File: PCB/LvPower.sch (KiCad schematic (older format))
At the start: 19 parts

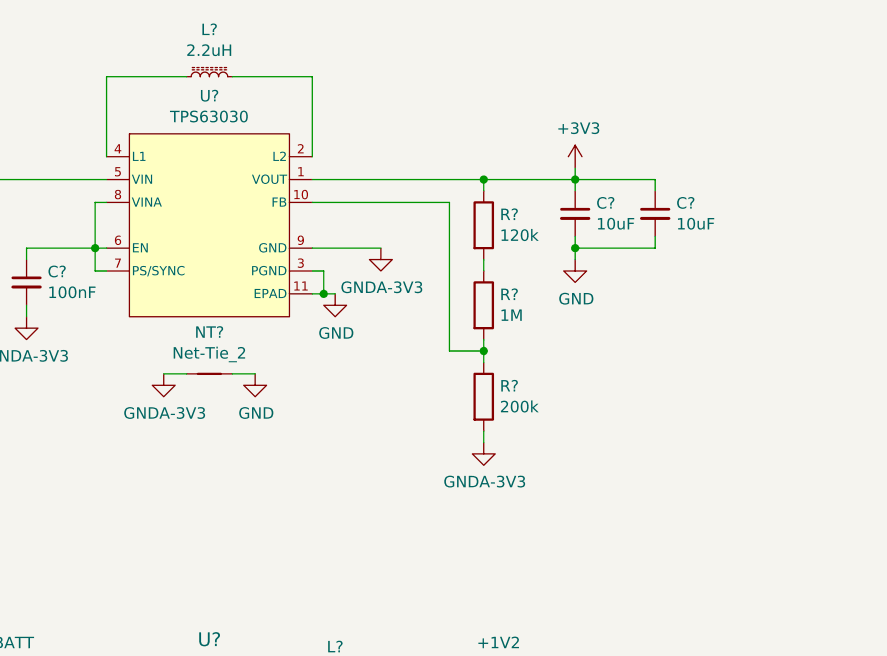
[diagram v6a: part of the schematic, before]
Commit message: Change TPS63030 to TPS63031 to reduce complexity
Parts are the same family, same footprint, same cost, but TPS63031 is a fixed 3.3V version, so it saves us a resistor divider.
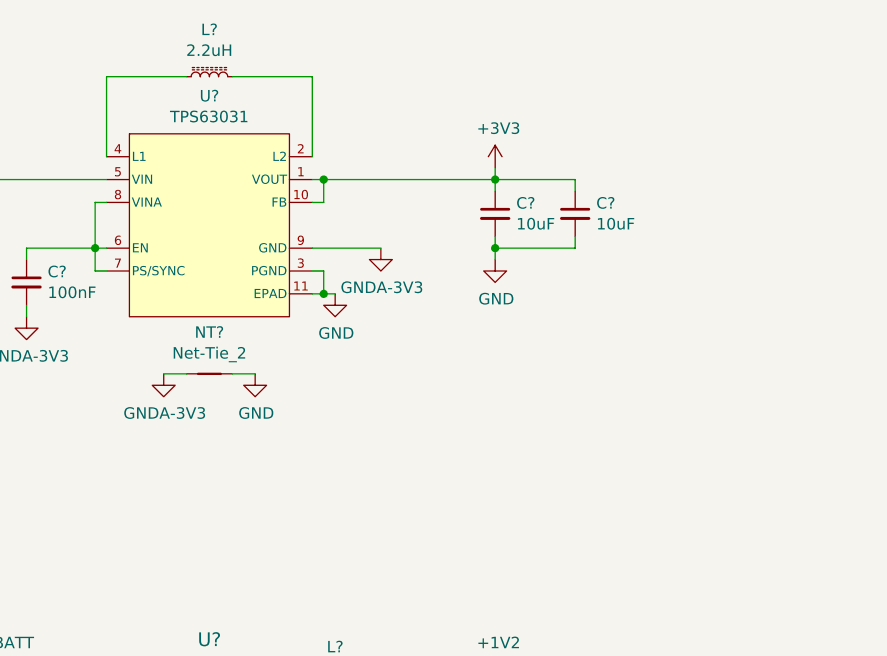
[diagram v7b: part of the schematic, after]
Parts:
- removed R?: 200k, Resistors_SMD:R_0603_HandSoldering, symbol Device:R
- removed R?: 1M, Resistors_SMD:R_0805_HandSoldering, symbol Device:R
- removed R?: 120k, Resistors_SMD:R_0805_HandSoldering, symbol Device:R
- removed U?: TPS63030, Parts:WSON10-PAD, symbol Parts:TPS63030
- added U?: TPS63031, Parts:WSON10-PAD, symbol Parts:TPS63031
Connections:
- net +3V3: now also U?.1 (VOUT), U?.10 (FB)
- net +BATT: now also U?.5 (VIN)
- net GND: now also U?.11 (EPAD), U?.3 (PGND)
- net GNDA-3V3: now also U?.9 (GND)
- net at L?.2: now also U?.2 (L2)
- net at L?.1: now also U?.4 (L1)
- net at C?.1: now also U?.6 (EN), U?.7 (PS/SYNC), U?.8 (VINA)
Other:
- moved on the sheet: C?
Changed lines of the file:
@@
 $EndComp
-Wire Wire Line
-	5250 3250 5250 3300
-Connection ~ 5250 3250
-Wire Wire Line
-	5100 3250 5250 3250
 Wire Wire Line
 	3250 3050 3250 3100
@@
 	1    0    0    -1
 $EndComp
-Connection ~ 5250 2500
-Wire Wire Line
-	5250 2500 5650 2500
-Wire Wire Line
-	5650 2750 5650 2800
-Wire Wire Line
-	5250 2500 5250 2550
-Wire Wire Line
-	5650 2500 5650 2550
-Connection ~ 5650 2500
-Wire Wire Line
-	5650 2450 5650 2500
+Wire Wire Line
+	5300 2750 5300 2800
+Wire Wire Line
+	5300 2500 5300 2550
+Connection ~ 5300 2500
+Wire Wire Line
+	5300 2450 5300 2500
 Wire Wire Line
 	2600 2500 2600 2550
@@
 Connection ~ 3550 2800
 Wire Wire Line
-	3550 2900 3600 2900
-Wire Wire Line
-	3550 2800 3550 2900
-Wire Wire Line
 	3550 2800 3600 2800
 Wire Wire Line
@@
 Wire Wire Line
 	3600 2600 3550 2600
-Wire Wire Line
-	5250 3200 5250 3250
-$Comp
-L Device:R R?
-U 1 1 5DCFE76B
-P 5250 3050
-F 0 "R?" H 5320 3096 50  0000 L CNN
-F 1 "1M" H 5320 3005 50  0000 L CNN
-F 2 "Resistors_SMD:R_0805_HandSoldering" V 5180 3050 50  0001 C CNN
-F 3 "https://www.digikey.ca/product-detail/en/panasonic-electronic-components/ERA-6AEB105V/P1MDACT-ND/1466019" H 5250 3050 50  0001 C CNN
-	1    5250 3050
-	1    0    0    -1
-$EndComp
-$Comp
-L Device:R R?
-U 1 1 5DCFD0C2
-P 5250 3450
-F 0 "R?" H 5320 3496 50  0000 L CNN
-F 1 "200k" H 5320 3405 50  0000 L CNN
-F 2 "Resistors_SMD:R_0603_HandSoldering" V 5180 3450 50  0001 C CNN
-F 3 "https://www.digikey.ca/product-detail/en/panasonic-electronic-components/ERA-3AEB204V/P200KDBCT-ND/1466107" H 5250 3450 50  0001 C CNN
-	1    5250 3450
-	1    0    0    -1
-$EndComp
 Wire Wire Line
 	4550 3000 4600 3000
@@
 Wire Wire Line
 	4500 3000 4550 3000
-$Comp
-L Parts:TPS63030 U?
-U 1 1 5DCF7F00
-P 4050 2700
-F 0 "U?" H 4050 3265 50  0000 C CNN
-F 1 "TPS63030" H 4050 3174 50  0000 C CNN
-F 2 "Parts:WSON10-PAD" H 4050 2250 60  0001 C CNN
-F 3 "http://www.ti.com/product/TPS63030" H 3600 2600 60  0001 C CNN
-	1    4050 2700
-	1    0    0    -1
-$EndComp
 $Comp
 L power:+BATT #PWR0103
@@
 L power:+3V3 #PWR0104
 U 1 1 5DCD8EE2
-P 5650 2450
-F 0 "#PWR0104" H 5650 2300 50  0001 C CNN
-F 1 "+3V3" H 5665 2623 50  0000 C CNN
-F 2 "" H 5650 2450 50  0001 C CNN
-F 3 "" H 5650 2450 50  0001 C CNN
-	1    5650 2450
+P 5300 2450
+F 0 "#PWR0104" H 5300 2300 50  0001 C CNN
+F 1 "+3V3" H 5315 2623 50  0000 C CNN
+F 2 "" H 5300 2450 50  0001 C CNN
+F 3 "" H 5300 2450 50  0001 C CNN
+	1    5300 2450
 	1    0    0    -1
 $EndComp
@@
 	1    0    0    -1
 $EndComp
-Wire Wire Line
-	5250 3650 5250 3600
 $Comp
 L Parts:GNDA-3V3 #PWR0106
@@
 $EndComp
 $Comp
-L Parts:GNDA-3V3 #PWR0108
-U 1 1 5DD4F61F
-P 5250 3650
-F 0 "#PWR0108" H 5250 3400 50  0001 C CNN
-F 1 "GNDA-3V3" H 5255 3477 50  0000 C CNN
-F 2 "" H 5250 3650 50  0001 C CNN
-F 3 "" H 5250 3650 50  0001 C CNN
-	1    5250 3650
-	1    0    0    -1
-$EndComp
-$Comp
 L Parts:GNDA-3V3 #PWR0109
 U 1 1 5DD4FC46
@@
 L power:GND #PWR0110
 U 1 1 5DD501DF
-P 5650 2850
-F 0 "#PWR0110" H 5650 2600 50  0001 C CNN
-F 1 "GND" H 5655 2677 50  0000 C CNN
-F 2 "" H 5650 2850 50  0001 C CNN
-F 3 "" H 5650 2850 50  0001 C CNN
-	1    5650 2850
+P 5300 2850
+F 0 "#PWR0110" H 5300 2600 50  0001 C CNN
+F 1 "GND" H 5305 2677 50  0000 C CNN
+F 2 "" H 5300 2850 50  0001 C CNN
+F 3 "" H 5300 2850 50  0001 C CNN
+	1    5300 2850
 	1    0    0    -1
 $EndComp
@@
 L Device:C_Small C?
 U 1 1 5DD59F79
-P 5650 2650
-F 0 "C?" H 5742 2696 50  0000 L CNN
-F 1 "10uF" H 5742 2605 50  0000 L CNN
-F 2 "Capacitors_SMD:C_0805_HandSoldering" H 5650 2650 50  0001 C CNN
-F 3 "https://www.digikey.ca/product-detail/en/kemet/C0805C106K8PACTU/399-4925-1-ND/1090920" H 5650 2650 50  0001 C CNN
-	1    5650 2650
+P 5300 2650
+F 0 "C?" H 5392 2696 50  0000 L CNN
+F 1 "10uF" H 5392 2605 50  0000 L CNN
+F 2 "Capacitors_SMD:C_0805_HandSoldering" H 5300 2650 50  0001 C CNN
+F 3 "https://www.digikey.ca/product-detail/en/kemet/C0805C106K8PACTU/399-4925-1-ND/1090920" H 5300 2650 50  0001 C CNN
+	1    5300 2650
 	1    0    0    -1
 $EndComp
@@
 L Device:C_Small C?
 U 1 1 5DD5CD9A
-P 6000 2650
-F 0 "C?" H 6092 2696 50  0000 L CNN
-F 1 "10uF" H 6092 2605 50  0000 L CNN
-F 2 "Capacitors_SMD:C_0805_HandSoldering" H 6000 2650 50  0001 C CNN
-F 3 "https://www.digikey.ca/product-detail/en/kemet/C0805C106K8PACTU/399-4925-1-ND/1090920" H 6000 2650 50  0001 C CNN
-	1    6000 2650
-	1    0    0    -1
-$EndComp
-Wire Wire Line
-	5650 2500 6000 2500
-Wire Wire Line
-	6000 2500 6000 2550
-Wire Wire Line
-	6000 2750 6000 2800
-Wire Wire Line
-	6000 2800 5650 2800
-Connection ~ 5650 2800
-Wire Wire Line
-	5650 2850 5650 2800
+P 5650 2650
+F 0 "C?" H 5742 2696 50  0000 L CNN
+F 1 "10uF" H 5742 2605 50  0000 L CNN
+F 2 "Capacitors_SMD:C_0805_HandSoldering" H 5650 2650 50  0001 C CNN
+F 3 "https://www.digikey.ca/product-detail/en/kemet/C0805C106K8PACTU/399-4925-1-ND/1090920" H 5650 2650 50  0001 C CNN
+	1    5650 2650
+	1    0    0    -1
+$EndComp
+Wire Wire Line
+	5300 2500 5650 2500
+Wire Wire Line
+	5650 2500 5650 2550
+Wire Wire Line
+	5650 2750 5650 2800
+Wire Wire Line
+	5650 2800 5300 2800
+Connection ~ 5300 2800
+Wire Wire Line
+	5300 2850 5300 2800
 Wire Wire Line
 	5300 5000 5300 5050
@@
 Wire Wire Line
 	4500 2050 4500 2400
-Wire Wire Line
-	4500 2500 5250 2500
-Wire Wire Line
-	4500 2600 5100 2600
-$Comp
-L Device:R R?
-U 1 1 5DDE565F
-P 5250 2700
-F 0 "R?" H 5320 2746 50  0000 L CNN
-F 1 "120k" H 5320 2655 50  0000 L CNN
-F 2 "Resistors_SMD:R_0805_HandSoldering" V 5180 2700 50  0001 C CNN
-F 3 "https://www.digikey.ca/product-detail/en/panasonic-electronic-components/ERA-6AED124V/P123803CT-ND/9467732" H 5250 2700 50  0001 C CNN
-	1    5250 2700
-	1    0    0    -1
-$EndComp
-Wire Wire Line
-	5250 2850 5250 2900
-Wire Wire Line
-	5100 2600 5100 3250
 $Comp
 L Parts:TCR2EF25 U?
@@
 	0    -1   -1   0
 $EndComp
+Wire Wire Line
+	3550 2900 3600 2900
+Wire Wire Line
+	3550 2800 3550 2900
+Wire Wire Line
+	4500 2500 4550 2500
+Wire Wire Line
+	4500 2600 4550 2600
+Wire Wire Line
+	4550 2600 4550 2500
+Wire Wire Line
+	4550 2500 5300 2500
+Connection ~ 4550 2500
+$Comp
+L Parts:TPS63031 U?
+U 1 1 5DDC16A1
+P 4050 2700
+F 0 "U?" H 4050 3265 50  0000 C CNN
+F 1 "TPS63031" H 4050 3174 50  0000 C CNN
+F 2 "Parts:WSON10-PAD" H 4050 2250 60  0001 C CNN
+F 3 "http://www.ti.com/product/TPS63031" H 3600 2600 60  0001 C CNN
+	1    4050 2700
+	1    0    0    -1
+$EndComp
 $EndSCHEMATC

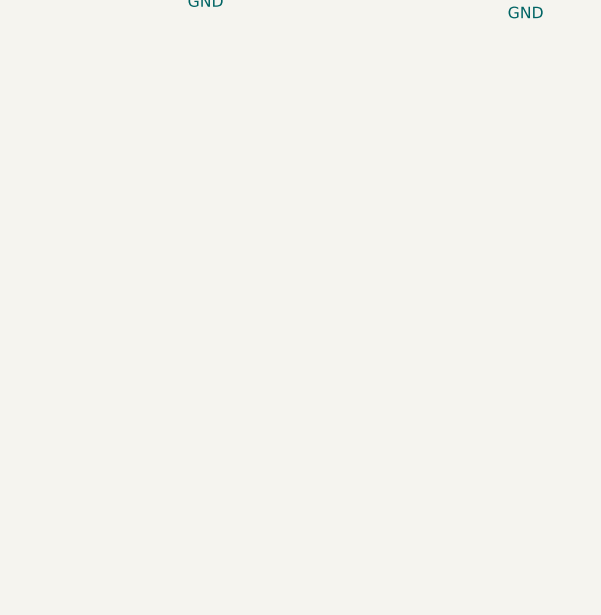
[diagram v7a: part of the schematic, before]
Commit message: Added low-noise supply rails, changed 100nF capacitors to 0603 footprint, fixed ENS210 footprint, added decoupling capacitors to microcontroller
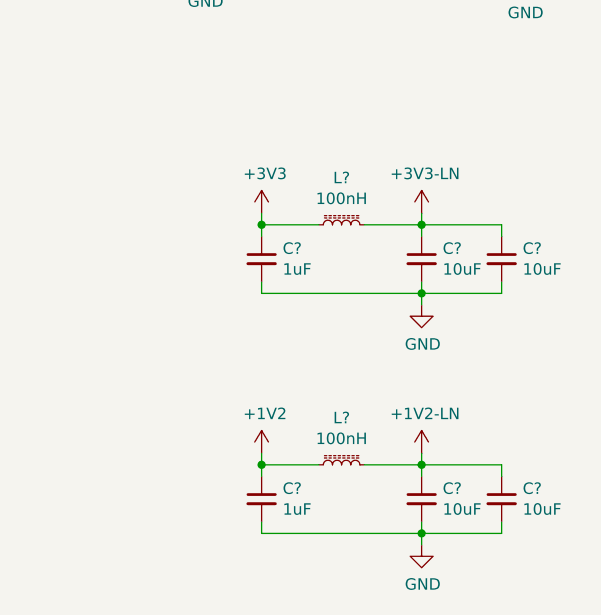
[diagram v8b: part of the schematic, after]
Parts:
- added C? (x4): 10uF, Capacitors_SMD:C_0805_HandSoldering, symbol Device:C_Small
- added C? (x2): 1uF, Capacitors_SMD:C_0603_HandSoldering, symbol Device:C_Small
- added L? (x2): 100nH, Resistors_SMD:R_0805_HandSoldering, symbol Device:L_Core_Ferrite_Small
- C?: footprint Capacitors_SMD:C_0402 -> Capacitors_SMD:C_0603_HandSoldering
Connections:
- net +1V2: now also C?.1, L?.1
- net +3V3: now also C?.1, L?.1
- net GND: now also C?.2, C?.2, C?.2, C?.2, C?.2, C?.2
- new net +1V2-LN: C?.1, C?.1, L?.2
- new net +3V3-LN: C?.1, C?.1, L?.2
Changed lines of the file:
@@
 F 0 "C?" H 3342 2996 50  0000 L CNN
 F 1 "100nF" H 3342 2905 50  0000 L CNN
-F 2 "Capacitors_SMD:C_0402" H 3250 2950 50  0001 C CNN
-F 3 "https://www.digikey.ca/product-detail/en/w-rth-elektronik/885012105010/732-7487-1-ND/5454114" H 3250 2950 50  0001 C CNN
+F 2 "Capacitors_SMD:C_0603_HandSoldering" H 3250 2950 50  0001 C CNN
+F 3 "https://www.digikey.ca/product-detail/en/w-rth-elektronik/885012206020/732-7939-1-ND/5454566" H 3250 2950 50  0001 C CNN
 	1    3250 2950
 	1    0    0    -1
@@
 	1    0    0    -1
 $EndComp
+$Comp
+L Parts:+3V3-LN #PWR?
+U 1 1 5DD3C0A0
+P 8250 4200
+F 0 "#PWR?" H 8250 4050 50  0001 C CNN
+F 1 "+3V3-LN" H 8265 4373 50  0000 C CNN
+F 2 "" H 8250 4200 50  0001 C CNN
+F 3 "" H 8250 4200 50  0001 C CNN
+	1    8250 4200
+	1    0    0    -1
+$EndComp
+$Comp
+L power:+3V3 #PWR?
+U 1 1 5DD3E19F
+P 7550 4200
+F 0 "#PWR?" H 7550 4050 50  0001 C CNN
+F 1 "+3V3" H 7565 4373 50  0000 C CNN
+F 2 "" H 7550 4200 50  0001 C CNN
+F 3 "" H 7550 4200 50  0001 C CNN
+	1    7550 4200
+	1    0    0    -1
+$EndComp
+$Comp
+L Device:C_Small C?
+U 1 1 5DD3EB70
+P 8250 4400
+F 0 "C?" H 8342 4446 50  0000 L CNN
+F 1 "10uF" H 8342 4355 50  0000 L CNN
+F 2 "Capacitors_SMD:C_0805_HandSoldering" H 8250 4400 50  0001 C CNN
+F 3 "https://www.digikey.ca/product-detail/en/kemet/C0805C106K8PACTU/399-4925-1-ND/1090920" H 8250 4400 50  0001 C CNN
+	1    8250 4400
+	1    0    0    -1
+$EndComp
+Wire Wire Line
+	8250 4200 8250 4250
+$Comp
+L Device:C_Small C?
+U 1 1 5DD417D3
+P 8600 4400
+F 0 "C?" H 8692 4446 50  0000 L CNN
+F 1 "10uF" H 8692 4355 50  0000 L CNN
+F 2 "Capacitors_SMD:C_0805_HandSoldering" H 8600 4400 50  0001 C CNN
+F 3 "https://www.digikey.ca/product-detail/en/kemet/C0805C106K8PACTU/399-4925-1-ND/1090920" H 8600 4400 50  0001 C CNN
+	1    8600 4400
+	1    0    0    -1
+$EndComp
+Wire Wire Line
+	8250 4250 8600 4250
+Wire Wire Line
+	8600 4250 8600 4300
+Connection ~ 8250 4250
+Wire Wire Line
+	8250 4250 8250 4300
+Wire Wire Line
+	8600 4500 8600 4550
+Wire Wire Line
+	8600 4550 8250 4550
+Wire Wire Line
+	8250 4550 8250 4500
+$Comp
+L power:GND #PWR?
+U 1 1 5DD45711
+P 8250 4600
+F 0 "#PWR?" H 8250 4350 50  0001 C CNN
+F 1 "GND" H 8255 4427 50  0000 C CNN
+F 2 "" H 8250 4600 50  0001 C CNN
+F 3 "" H 8250 4600 50  0001 C CNN
+	1    8250 4600
+	1    0    0    -1
+$EndComp
+Wire Wire Line
+	8250 4600 8250 4550
+Connection ~ 8250 4550
+$Comp
+L Device:L_Core_Ferrite_Small L?
+U 1 1 5DD48EC8
+P 7900 4250
+F 0 "L?" V 8105 4250 50  0000 C CNN
+F 1 "100nH" V 8014 4250 50  0000 C CNN
+F 2 "Resistors_SMD:R_0805_HandSoldering" H 7900 4250 50  0001 C CNN
+F 3 "https://www.digikey.ca/product-detail/en/tdk-corporation/MLZ2012DR10DT000/445-6395-1-ND/2465721" H 7900 4250 50  0001 C CNN
+	1    7900 4250
+	0    -1   -1   0
+$EndComp
+Wire Wire Line
+	8000 4250 8250 4250
+Wire Wire Line
+	7800 4250 7550 4250
+Wire Wire Line
+	7550 4250 7550 4200
+$Comp
+L Device:C_Small C?
+U 1 1 5DD59CF4
+P 7550 4400
+F 0 "C?" H 7642 4446 50  0000 L CNN
+F 1 "1uF" H 7642 4355 50  0000 L CNN
+F 2 "Capacitors_SMD:C_0603_HandSoldering" H 7550 4400 50  0001 C CNN
+F 3 "https://www.digikey.ca/product-detail/en/samsung-electro-mechanics/CL10A105MP8NNNC/1276-1866-1-ND/3889952" H 7550 4400 50  0001 C CNN
+	1    7550 4400
+	1    0    0    -1
+$EndComp
+Wire Wire Line
+	7550 4300 7550 4250
+Connection ~ 7550 4250
+Wire Wire Line
+	7550 4500 7550 4550
+Wire Wire Line
+	7550 4550 8250 4550
+$Comp
+L Device:C_Small C?
+U 1 1 5DD65CDB
+P 8250 5450
+F 0 "C?" H 8342 5496 50  0000 L CNN
+F 1 "10uF" H 8342 5405 50  0000 L CNN
+F 2 "Capacitors_SMD:C_0805_HandSoldering" H 8250 5450 50  0001 C CNN
+F 3 "https://www.digikey.ca/product-detail/en/kemet/C0805C106K8PACTU/399-4925-1-ND/1090920" H 8250 5450 50  0001 C CNN
+	1    8250 5450
+	1    0    0    -1
+$EndComp
+Wire Wire Line
+	8250 5250 8250 5300
+$Comp
+L Device:C_Small C?
+U 1 1 5DD65CE6
+P 8600 5450
+F 0 "C?" H 8692 5496 50  0000 L CNN
+F 1 "10uF" H 8692 5405 50  0000 L CNN
+F 2 "Capacitors_SMD:C_0805_HandSoldering" H 8600 5450 50  0001 C CNN
+F 3 "https://www.digikey.ca/product-detail/en/kemet/C0805C106K8PACTU/399-4925-1-ND/1090920" H 8600 5450 50  0001 C CNN
+	1    8600 5450
+	1    0    0    -1
+$EndComp
+Wire Wire Line
+	8250 5300 8600 5300
+Wire Wire Line
+	8600 5300 8600 5350
+Connection ~ 8250 5300
+Wire Wire Line
+	8250 5300 8250 5350
+Wire Wire Line
+	8600 5550 8600 5600
+Wire Wire Line
+	8600 5600 8250 5600
+Wire Wire Line
+	8250 5600 8250 5550
+$Comp
+L power:GND #PWR?
+U 1 1 5DD65CF7
+P 8250 5650
+F 0 "#PWR?" H 8250 5400 50  0001 C CNN
+F 1 "GND" H 8255 5477 50  0000 C CNN
+F 2 "" H 8250 5650 50  0001 C CNN
+F 3 "" H 8250 5650 50  0001 C CNN
+	1    8250 5650
+	1    0    0    -1
+$EndComp
+Wire Wire Line
+	8250 5650 8250 5600
+Connection ~ 8250 5600
+$Comp
+L Device:L_Core_Ferrite_Small L?
+U 1 1 5DD65D03
+P 7900 5300
+F 0 "L?" V 8105 5300 50  0000 C CNN
+F 1 "100nH" V 8014 5300 50  0000 C CNN
+F 2 "Resistors_SMD:R_0805_HandSoldering" H 7900 5300 50  0001 C CNN
+F 3 "https://www.digikey.ca/product-detail/en/tdk-corporation/MLZ2012DR10DT000/445-6395-1-ND/2465721" H 7900 5300 50  0001 C CNN
+	1    7900 5300
+	0    -1   -1   0
+$EndComp
+Wire Wire Line
+	8000 5300 8250 5300
+Wire Wire Line
+	7800 5300 7550 5300
+Wire Wire Line
+	7550 5300 7550 5250
+$Comp
+L Device:C_Small C?
+U 1 1 5DD65D10
+P 7550 5450
+F 0 "C?" H 7642 5496 50  0000 L CNN
+F 1 "1uF" H 7642 5405 50  0000 L CNN
+F 2 "Capacitors_SMD:C_0603_HandSoldering" H 7550 5450 50  0001 C CNN
+F 3 "https://www.digikey.ca/product-detail/en/samsung-electro-mechanics/CL10A105MP8NNNC/1276-1866-1-ND/3889952" H 7550 5450 50  0001 C CNN
+	1    7550 5450
+	1    0    0    -1
+$EndComp
+Wire Wire Line
+	7550 5350 7550 5300
+Connection ~ 7550 5300
+Wire Wire Line
+	7550 5550 7550 5600
+Wire Wire Line
+	7550 5600 8250 5600
+$Comp
+L power:+1V2 #PWR?
+U 1 1 5DD6DA7B
+P 7550 5250
+F 0 "#PWR?" H 7550 5100 50  0001 C CNN
+F 1 "+1V2" H 7565 5423 50  0000 C CNN
+F 2 "" H 7550 5250 50  0001 C CNN
+F 3 "" H 7550 5250 50  0001 C CNN
+	1    7550 5250
+	1    0    0    -1
+$EndComp
+$Comp
+L Parts:+1V2-LN #PWR?
+U 1 1 5DD6F7D4
+P 8250 5250
+F 0 "#PWR?" H 8250 5100 50  0001 C CNN
+F 1 "+1V2-LN" H 8265 5423 50  0000 C CNN
+F 2 "" H 8250 5250 50  0001 C CNN
+F 3 "" H 8250 5250 50  0001 C CNN
+	1    8250 5250
+	1    0    0    -1
+$EndComp
